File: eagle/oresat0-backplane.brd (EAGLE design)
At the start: 82.5 x 99 mm, 49 parts, among them J1 5-104196-5, J3 HARWIN-M50-3501042

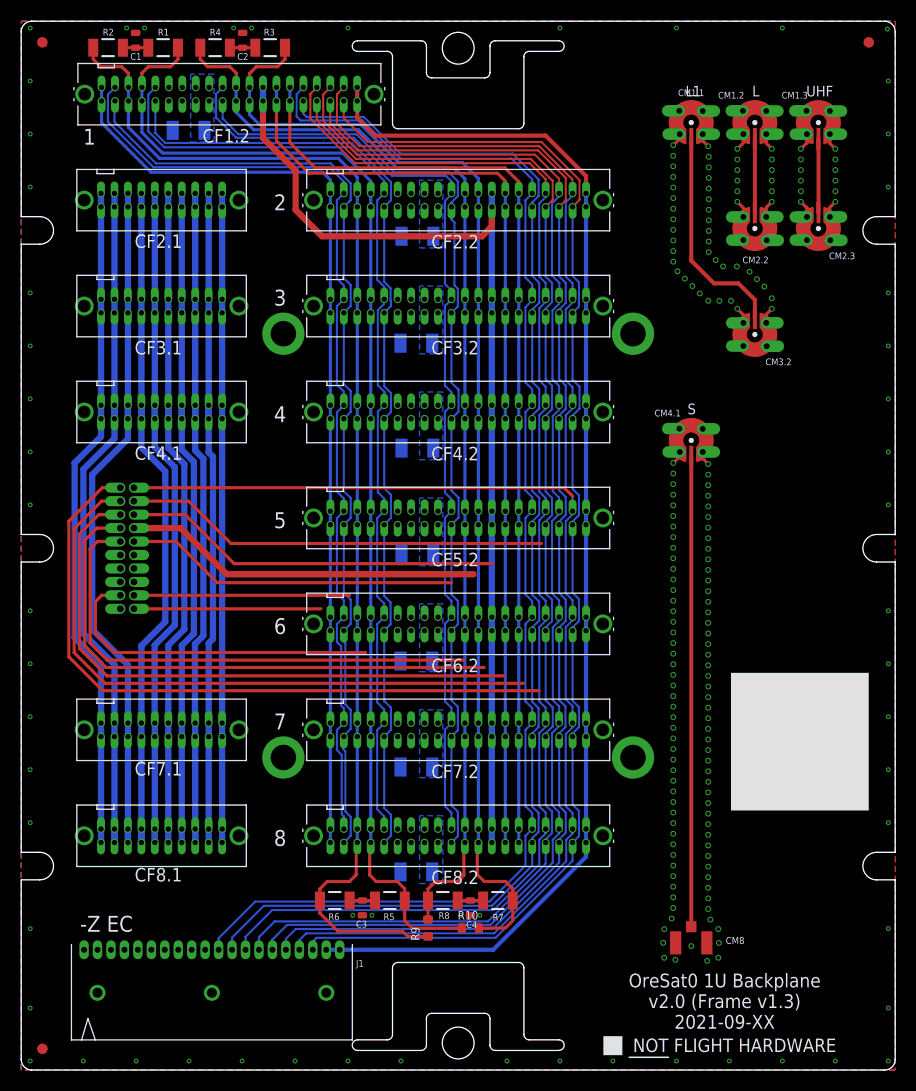
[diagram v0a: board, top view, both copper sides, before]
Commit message: Backplane v2.0. Changes to signals; vaguely back compatible with v1. Also spun off OreSat0 bespoke backplane for the OreSat0 mission.
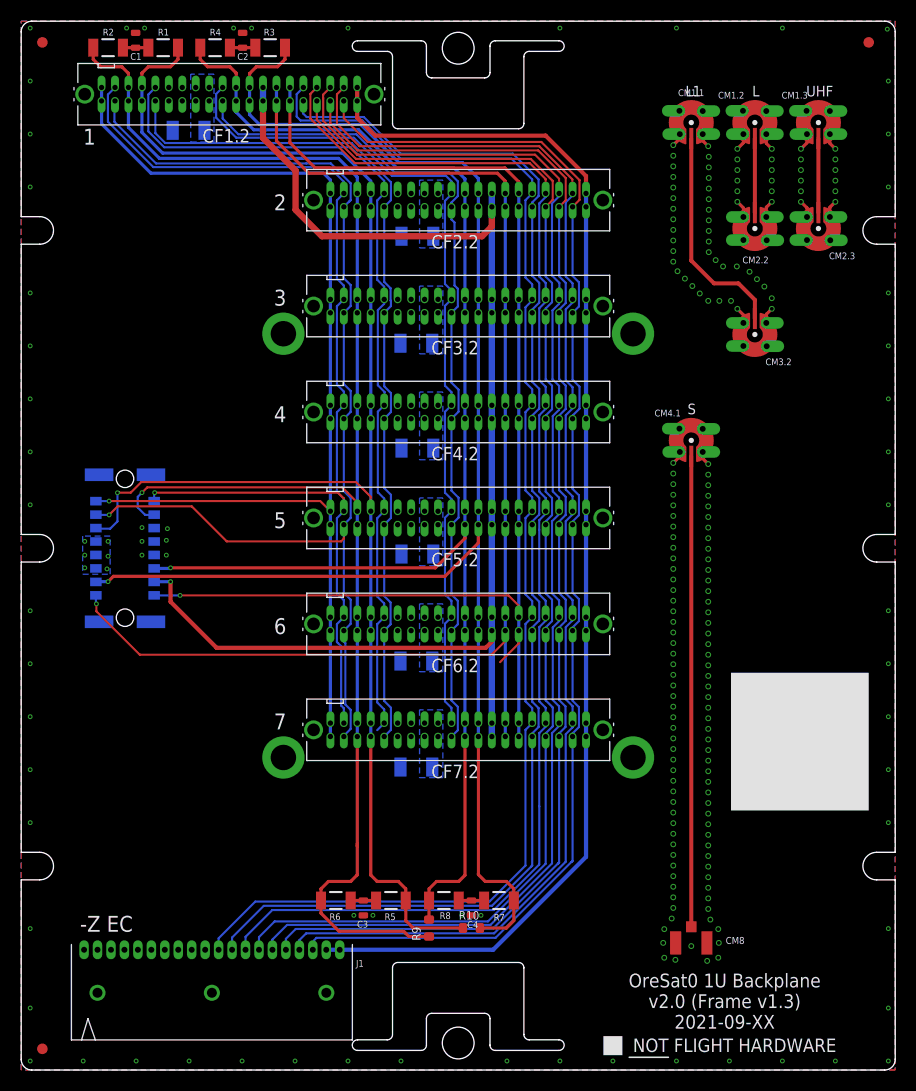
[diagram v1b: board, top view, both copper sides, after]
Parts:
- removed C12: (no value), oresat-rcl:1206-B
- removed CF2.1, CF3.1, CF4.1, CF7.1, CF8.1: SFM-110-X1-XXX-D-LC, J-Samtec-SFM-110-X1-XXX-D-LC:SFM-110-X1-XXX-D-LC
- removed CF8.2: SFM-120-X1-XXX-D, J-Samtec-SFM-120-X1-XXX-D:SFM-120-X1-XXX-D
- removed J3: HARWIN-M50-3501042, J-Harwin-M50-3501042-20pin-M-1.27mm-vertical-th:HARWIN-M50-3501042
- added J2: M55-6001642R, J-Harwin-M55-60X1642R-16pin-1.27mm-F-vertical:CONN_M55-6001642R_HRW
- moved C4 0.10 mm to (42.5, 15.3)
- moved R10 0.10 mm to (42.5, 13.4)
- moved R5 0.10 mm to (34.9, 16.0)
- moved R7 0.10 mm to (45.1, 16.0)
- moved R8 0.10 mm to (39.9, 16.0)
- moved R9 0.10 mm to (38.5, 13.4)
- moved R6 0.10 mm to (29.7, 16.0)
- moved C3 0.10 mm to (32.3, 15.3)
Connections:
- removed net AUX-1: CF2.1.1, CF2.1.2, CF3.1.1, CF3.1.2, CF4.1.1, CF4.1.2, CF7.1.1, CF7.1.2, CF8.1.1, CF8.1.2
- removed net AUX-10: CF2.1.19, CF2.1.20, CF3.1.19, CF3.1.20, CF4.1.19, CF4.1.20, CF7.1.19, CF7.1.20, CF8.1.19, CF8.1.20
- removed net AUX-2: CF2.1.3, CF2.1.4, CF3.1.3, CF3.1.4, CF4.1.3, CF4.1.4, CF7.1.3, CF7.1.4, CF8.1.3, CF8.1.4
- removed net AUX-3: CF2.1.5, CF2.1.6, CF3.1.5, CF3.1.6, CF4.1.5, CF4.1.6, CF7.1.5, CF7.1.6, CF8.1.5, CF8.1.6
- removed net AUX-4: CF2.1.7, CF2.1.8, CF3.1.7, CF3.1.8, CF4.1.7, CF4.1.8, CF7.1.7, CF7.1.8, CF8.1.7, CF8.1.8
- removed net AUX-5: CF2.1.10, CF2.1.9, CF3.1.10, CF3.1.9, CF4.1.10, CF4.1.9, CF7.1.10, CF7.1.9, CF8.1.10, CF8.1.9
- removed net AUX-6: CF2.1.11, CF2.1.12, CF3.1.11, CF3.1.12, CF4.1.11, CF4.1.12, CF7.1.11, CF7.1.12, CF8.1.11, CF8.1.12
- removed net AUX-7: CF2.1.13, CF2.1.14, CF3.1.13, CF3.1.14, CF4.1.13, CF4.1.14, CF7.1.13, CF7.1.14, CF8.1.13, CF8.1.14
- removed net AUX-8: CF2.1.15, CF2.1.16, CF3.1.15, CF3.1.16, CF4.1.15, CF4.1.16, CF7.1.15, CF7.1.16, CF8.1.15, CF8.1.16
- removed net AUX-9: CF2.1.17, CF2.1.18, CF3.1.17, CF3.1.18, CF4.1.17, CF4.1.18, CF7.1.17, CF7.1.18, CF8.1.17, CF8.1.18
- removed net SPARE1-TURNSTILE-DPLY: J3.5
- removed net SPARE2: J3.4
- removed net SPARE3-MAG-PWR: J3.3
- removed net SPARE4-MAG-SCL: J3.2
- removed net SPARE5-MAG-SDA: J3.1
- removed net UART-RX: CF1.2.38, CF2.2.38, CF3.2.38, CF4.2.38, CF5.2.38, CF6.2.38, CF7.2.38, CF8.2.38
- removed net UART-TX: CF1.2.37, CF2.2.37, CF3.2.37, CF4.2.37, CF5.2.37, CF6.2.37, CF7.2.37, CF8.2.37
- new net C3-UART-RX: CF1.2.38, CF2.2.38, CF3.2.38, CF4.2.38, CF5.2.38, CF6.2.38, CF7.2.38, J2.2
- new net C3-UART-TX: CF1.2.37, CF2.2.37, CF3.2.37, CF4.2.37, CF5.2.37, CF6.2.37, CF7.2.37, J2.3
- net !SD: now also J2.1; no longer CF8.2.39, CF8.2.40, J3.20
- net CAN1_H: now also J2.5; no longer CF8.2.33, CF8.2.34, J3.17
- net CAN1_L: now also J2.4; no longer CF8.2.35, CF8.2.36, J3.18
- net CAN2_H: now also J2.13; no longer CF8.2.17, CF8.2.18, J3.9
- net CAN2_L: now also J2.12; no longer CF8.2.19, CF8.2.20, J3.10
- net GND: now also J2.10, J2.19, J2.20, J2.21, J2.22, J2.6, J2.8; no longer C12.2, CF2.1.LC1, CF2.1.LC2, CF3.1.LC1, CF3.1.LC2, CF4.1.LC1, CF4.1.LC2, CF7.1.LC1, CF7.1.LC2, CF8.1.LC1, CF8.1.LC2, CF8.2.27, CF8.2.28, CF8.2.29, CF8.2.30, CF8.2.LC1, CF8.2.LC2, J3.14, J3.15, J3.16, J3.19
- net OPD_PWR: now also J2.14; no longer CF8.2.15, CF8.2.16, J3.8
- net OPD_SCL: now also J2.15; no longer CF8.2.13, CF8.2.14, J3.7
- net OPD_SDA: now also J2.16; no longer CF8.2.11, CF8.2.12, J3.6
- net SPARE1: no longer CF8.2.1, CF8.2.2
- net SPARE10: no longer CF8.2.10
- net SPARE21: no longer CF8.2.21
- net SPARE22: no longer CF8.2.22
- net SPARE3: no longer CF8.2.3
- net SPARE31: no longer CF8.2.31
- net SPARE32: no longer CF8.2.32
- net SPARE4: no longer CF8.2.4
- net SPARE5: no longer CF8.2.5
- net SPARE6: no longer CF8.2.6
- net SPARE7: no longer CF8.2.7
- net SPARE8: no longer CF8.2.8
- net SPARE9: no longer CF8.2.9
- net VBUS: now also J2.11, J2.7, J2.9; no longer C12.1, CF8.2.23, CF8.2.24, CF8.2.25, CF8.2.26, J3.11, J3.12, J3.13
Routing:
- net C3-UART-TX: track 0.00 -> 108.5 mm, vias 0 -> 1
- net C3-UART-RX: track 0.00 -> 102.0 mm, vias 0 -> 1
- net UART-RX: track 92.5 -> 0.00 mm
- net UART-TX: track 92.5 -> 0.00 mm
- net AUX-8: track 66.6 -> 0.00 mm
- net AUX-9: track 66.2 -> 0.00 mm
- net AUX-7: track 65.7 -> 0.00 mm
- net AUX-6: track 65.4 -> 0.00 mm
- net SPARE5-MAG-SDA: track 64.7 -> 0.00 mm
- net AUX-3: track 64.5 -> 0.00 mm
- net AUX-5: track 63.8 -> 0.00 mm
- net AUX-4: track 63.5 -> 0.00 mm
- net AUX-10: track 63.3 -> 0.00 mm
- net AUX-2: track 62.9 -> 0.00 mm
- net AUX-1: track 61.3 -> 0.00 mm
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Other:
- board text removed: "8"
